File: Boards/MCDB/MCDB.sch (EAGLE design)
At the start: 57 parts, among them IC1 MC33926

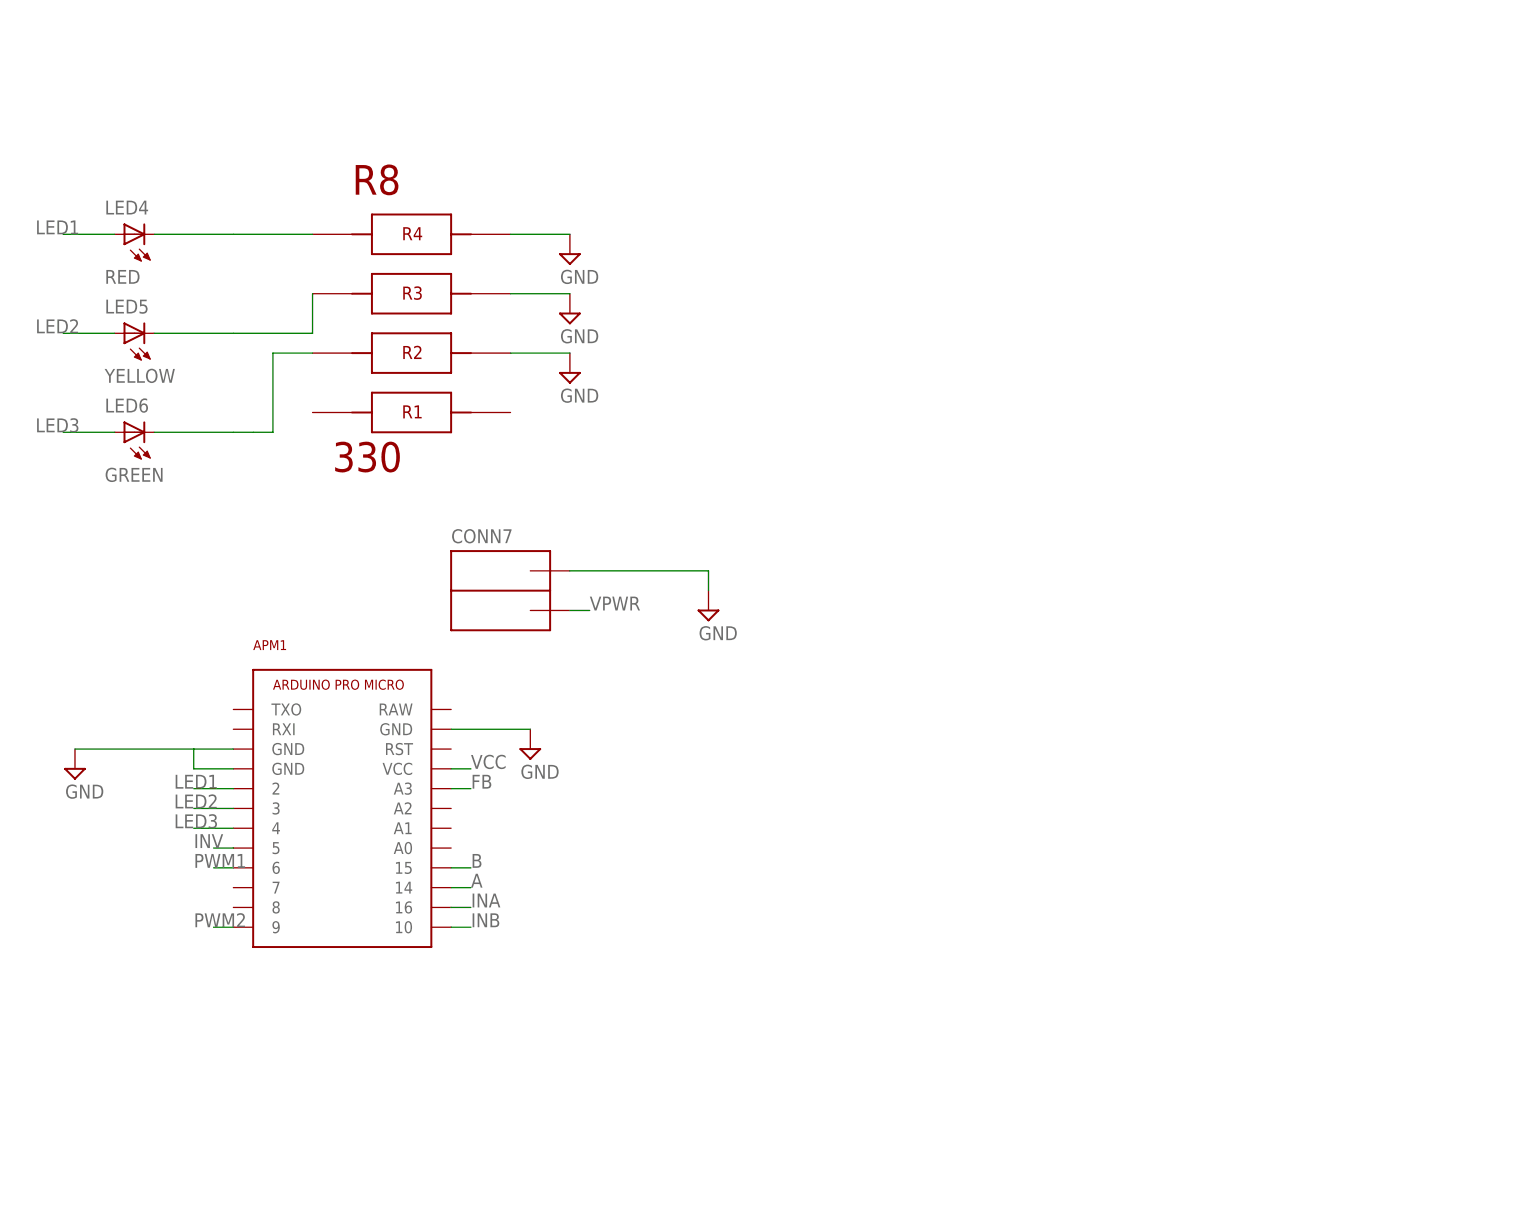
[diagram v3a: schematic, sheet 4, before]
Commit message: add 32U4 to mcdb schematic
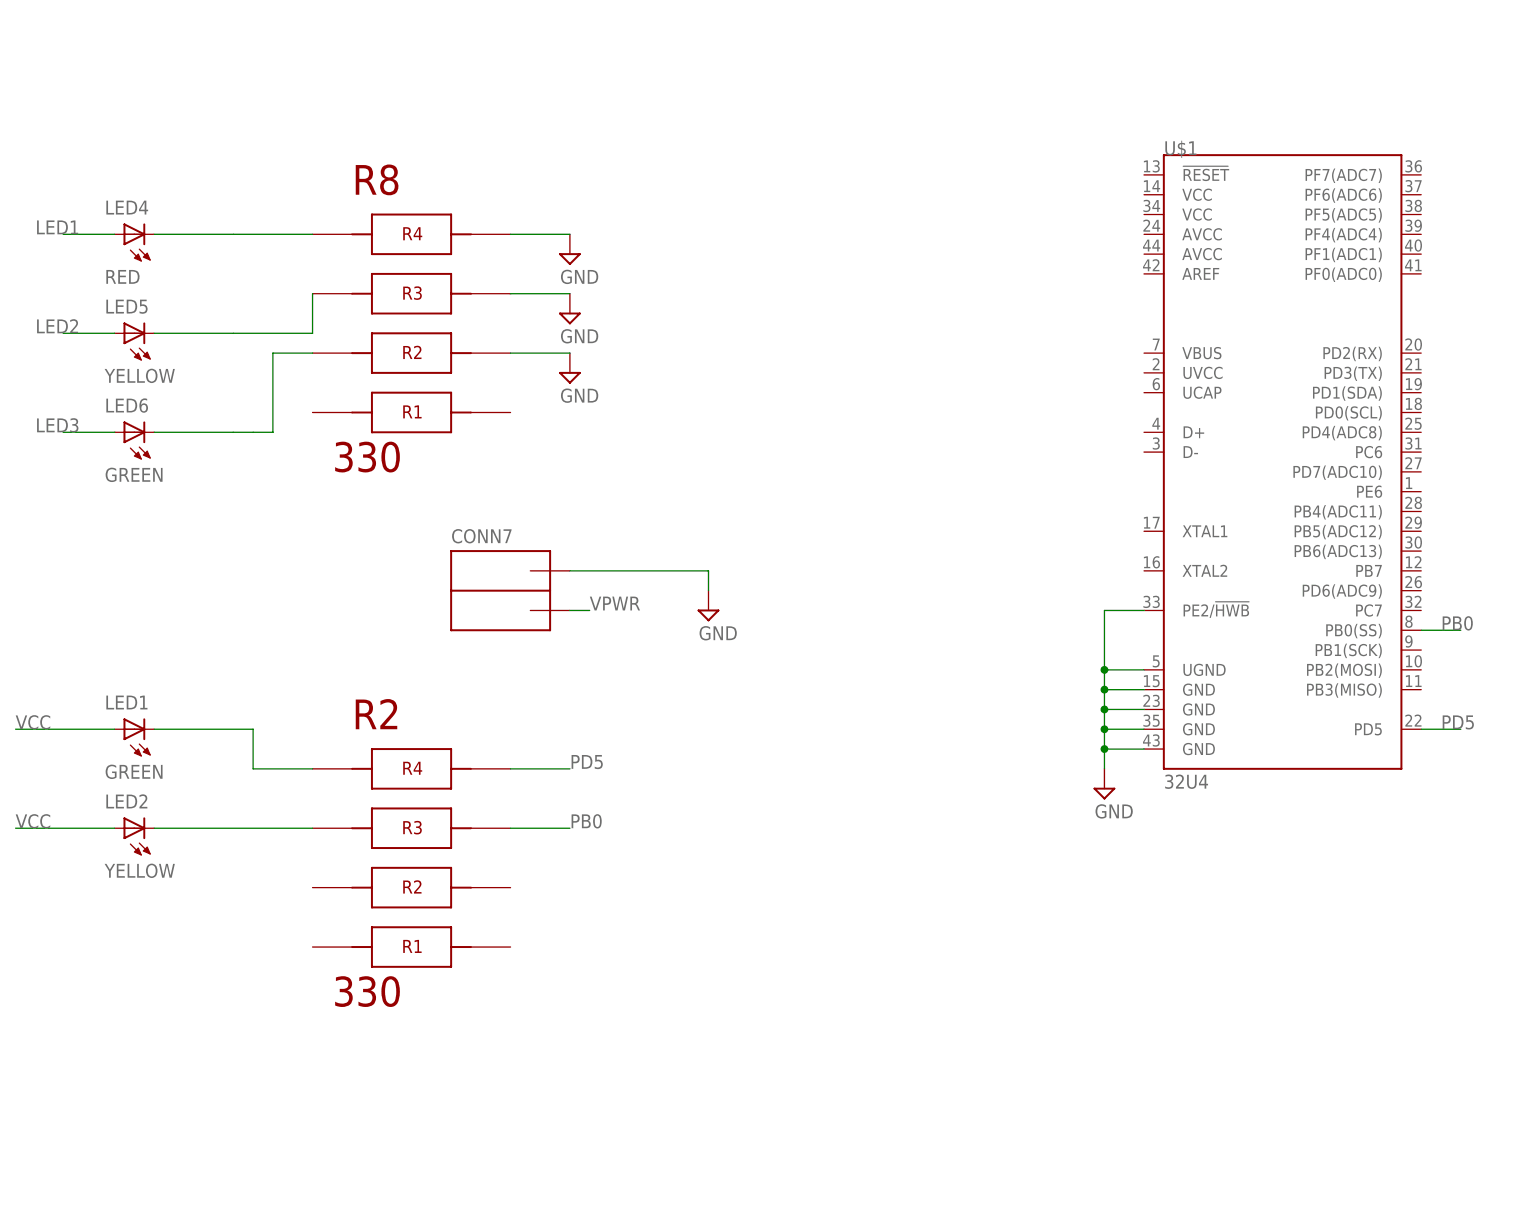
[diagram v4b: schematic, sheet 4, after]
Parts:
- removed APM1: ARDUINO_PRO_MICRO, pie:ARDUINO_PRO_MICRO
- added LED1: GREEN, pie:LED1206
- added LED2: YELLOW, pie:LED1206
- added R2: 330, pie:4X-0603
- added U$1: 32U4, SparkFun-IC-Microcontroller:ATMEGA32U4TQFP-44
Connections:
- removed net A: APM1.14
- removed net B: APM1.15
- removed net FB: APM1.A3
- removed net INA: APM1.16
- removed net INB: APM1.10
- removed net INV: APM1.5
- new net N$12: LED1.C, R2.5
- new net N$13: LED2.C, R2.6
- new net PB0: R2.3, U$1.PB0(SS)
- new net PD5: R2.4, U$1.PD5
- net GND: now also U$1.GND@15, U$1.GND@23, U$1.GND@35, U$1.GND@43, U$1.PE2/!HWB, U$1.UGND; no longer APM1.GND@0, APM1.GND@1, APM1.GND@2
- net LED1: no longer APM1.2
- net LED2: no longer APM1.3
- net LED3: no longer APM1.4
- net PWM1: no longer APM1.6
- net PWM2: no longer APM1.9
- net VCC: now also LED1.A, LED2.A; no longer APM1.VCC

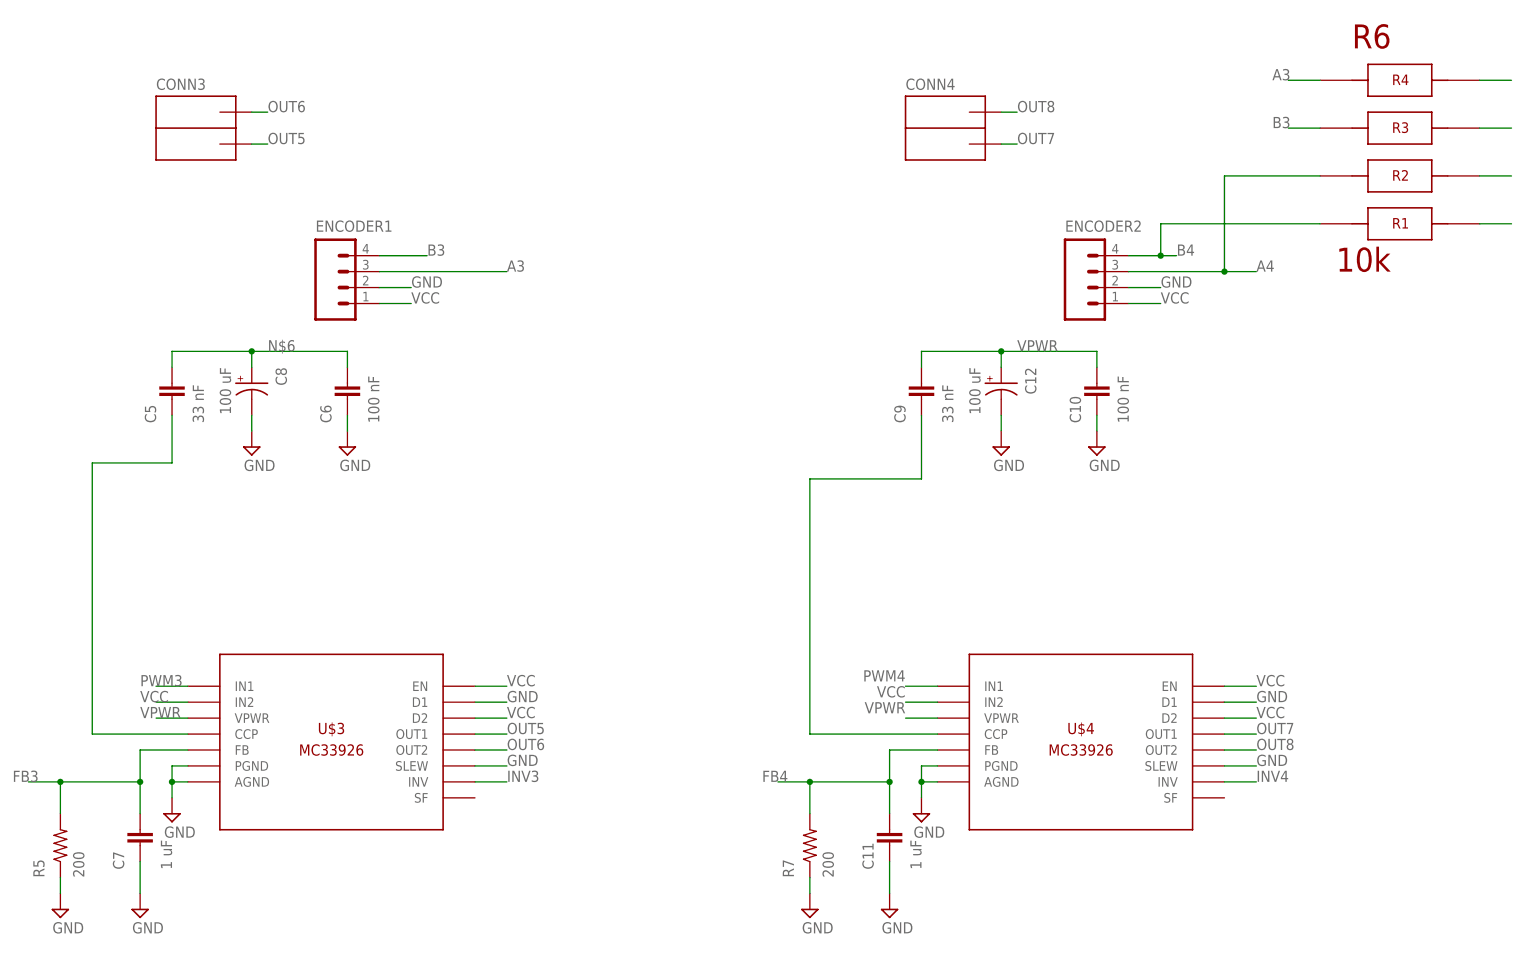
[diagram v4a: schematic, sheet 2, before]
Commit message: Added atmega32u4 to library
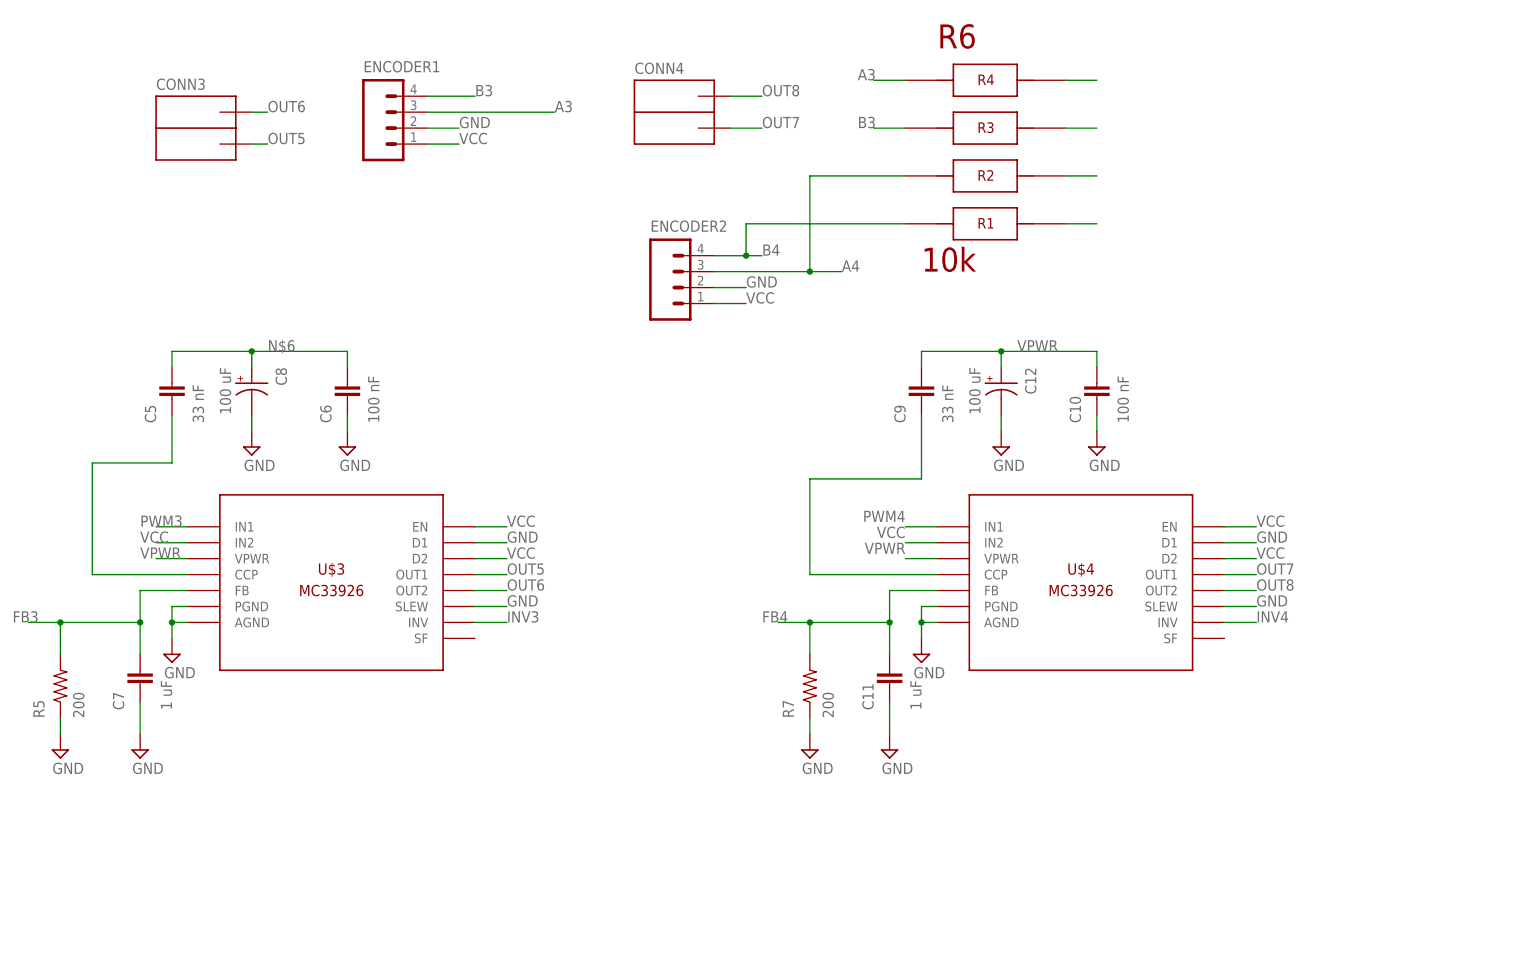
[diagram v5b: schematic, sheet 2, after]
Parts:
- U$1: device SparkFun-IC-Microcontroller:ATMEGA32U4TQFP-44 -> pie:ATMEGA32U4TQFP-44
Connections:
- new net N$16: U$1.VCC@14
- new net N$17: U$1.VCC@34
- new net N$18: U$1.AVCC@24
- new net N$19: U$1.AVCC@44
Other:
- moved on the sheet: C11, C15, C19, C23, C3, C7, CONN4, ENCODER1, ENCODER2, IC1, R11, R13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

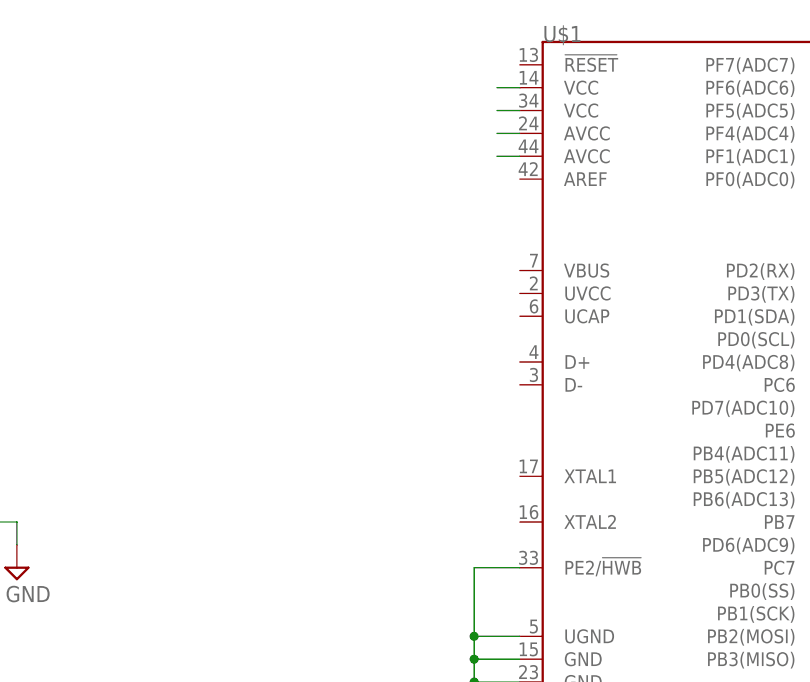
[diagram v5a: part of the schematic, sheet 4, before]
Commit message: added new crystal footprint
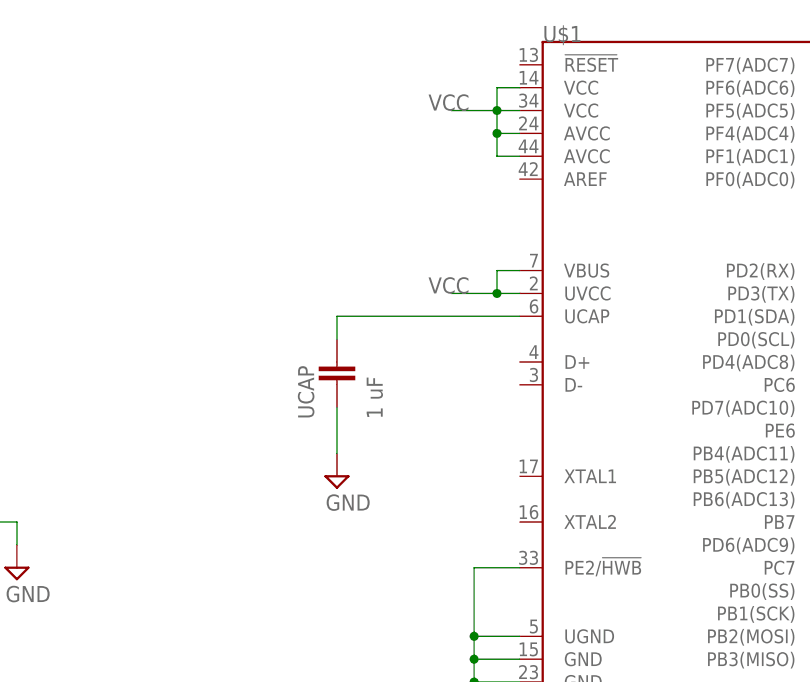
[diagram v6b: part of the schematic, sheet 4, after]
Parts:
- added UCAP: 1 uF, pie:CAP0603-CAP
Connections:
- removed net N$17: U$1.VCC@34
- removed net N$18: U$1.AVCC@24
- removed net N$19: U$1.AVCC@44
- net GND: now also UCAP.1
- net N$16: now also U$1.UCAP, UCAP.2; no longer U$1.VCC@14
- net VCC: now also U$1.AVCC@24, U$1.AVCC@44, U$1.UVCC, U$1.VBUS, U$1.VCC@14, U$1.VCC@34
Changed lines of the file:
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@@
 <part name="R2" library="pie" deviceset="4X-0603" device="" value="330"/>
 <part name="U$1" library="pie" deviceset="ATMEGA32U4" device="TQFP-44" package3d_urn="urn:adsk.eagle:package:38953/1" value="32U4"/>
+<part name="UCAP" library="pie" deviceset="CAP" device="0603-CAP" value="1 uF"/>
+<part name="SUPPLY15" library="pie" deviceset="GND" device=""/>
 </parts>
 <sheets>
@@
 <attribute name="NAME" x="157.48" y="160.02" size="1.778" layer="95"/>
 <attribute name="VALUE" x="157.48" y="78.74" size="1.778" layer="96"/>
+</instance>
+<instance part="UCAP" gate="G$1" x="134.62" y="121.92" smashed="yes" rot="R90">
+<attribute name="NAME" x="132.08" y="118.11" size="1.778" layer="95" rot="R90"/>
+<attribute name="VALUE" x="139.7" y="118.11" size="1.778" layer="96" rot="R90"/>
+</instance>
+<instance part="SUPPLY15" gate="GND" x="134.62" y="111.76" smashed="yes">
+<attribute name="VALUE" x="133.35" y="107.95" size="1.778" layer="96"/>
 </instance>
 </instances>
@@
 <pinref part="U$1" gate="G$1" pin="UGND"/>
 </segment>
+<segment>
+<pinref part="SUPPLY15" gate="GND" pin="GND"/>
+<pinref part="UCAP" gate="G$1" pin="1"/>
+<wire x1="134.62" y1="114.3" x2="134.62" y2="119.38" width="0.1524" layer="91"/>
+</segment>
 </net>
 <net name="LED1" class="0">
@@
 <label x="10.16" y="73.66" size="1.778" layer="95"/>
 </segment>
+<segment>
+<pinref part="U$1" gate="G$1" pin="AVCC@44"/>
+<wire x1="154.94" y1="147.32" x2="152.4" y2="147.32" width="0.1524" layer="91"/>
+<pinref part="U$1" gate="G$1" pin="AVCC@24"/>
+<wire x1="154.94" y1="149.86" x2="152.4" y2="149.86" width="0.1524" layer="91"/>
+<wire x1="152.4" y1="147.32" x2="152.4" y2="149.86" width="0.1524" layer="91"/>
+<pinref part="U$1" gate="G$1" pin="VCC@34"/>
+<wire x1="154.94" y1="152.4" x2="152.4" y2="152.4" width="0.1524" layer="91"/>
+<wire x1="152.4" y1="149.86" x2="152.4" y2="152.4" width="0.1524" layer="91"/>
+<junction x="152.4" y="149.86"/>
+<pinref part="U$1" gate="G$1" pin="VCC@14"/>
+<wire x1="154.94" y1="154.94" x2="152.4" y2="154.94" width="0.1524" layer="91"/>
+<wire x1="152.4" y1="152.4" x2="152.4" y2="154.94" width="0.1524" layer="91"/>
+<junction x="152.4" y="152.4"/>
+<wire x1="152.4" y1="152.4" x2="147.32" y2="152.4" width="0.1524" layer="91"/>
+<label x="144.78" y="152.4" size="1.778" layer="95"/>
+</segment>
+<segment>
+<pinref part="U$1" gate="G$1" pin="VBUS"/>
+<wire x1="154.94" y1="134.62" x2="152.4" y2="134.62" width="0.1524" layer="91"/>
+<pinref part="U$1" gate="G$1" pin="UVCC"/>
+<wire x1="154.94" y1="132.08" x2="152.4" y2="132.08" width="0.1524" layer="91"/>
+<wire x1="152.4" y1="132.08" x2="152.4" y2="134.62" width="0.1524" layer="91"/>
+<junction x="152.4" y="132.08"/>
+<wire x1="152.4" y1="132.08" x2="147.32" y2="132.08" width="0.1524" layer="91"/>
+<label x="144.78" y="132.08" size="1.778" layer="95"/>
+</segment>
 </net>
 <net name="PD5" class="0">
@@
 <net name="N$16" class="0">
 <segment>
-<pinref part="U$1" gate="G$1" pin="VCC@14"/>
-<wire x1="154.94" y1="154.94" x2="152.4" y2="154.94" width="0.1524" layer="91"/>
-</segment>
-</net>
-<net name="N$17" class="0">
-<segment>
-<pinref part="U$1" gate="G$1" pin="VCC@34"/>
-<wire x1="154.94" y1="152.4" x2="152.4" y2="152.4" width="0.1524" layer="91"/>
-</segment>
-</net>
-<net name="N$18" class="0">
-<segment>
-<pinref part="U$1" gate="G$1" pin="AVCC@24"/>
-<wire x1="154.94" y1="149.86" x2="152.4" y2="149.86" width="0.1524" layer="91"/>
-</segment>
-</net>
-<net name="N$19" class="0">
-<segment>
-<pinref part="U$1" gate="G$1" pin="AVCC@44"/>
-<wire x1="154.94" y1="147.32" x2="152.4" y2="147.32" width="0.1524" layer="91"/>
-</segment>
-</net>
+<pinref part="U$1" gate="G$1" pin="UCAP"/>
+<pinref part="UCAP" gate="G$1" pin="2"/>
+<wire x1="154.94" y1="129.54" x2="134.62" y2="129.54" width="0.1524" layer="91"/>
+<wire x1="134.62" y1="129.54" x2="134.62" y2="127" width="0.1524" layer="91"/>
+</segment>
+</net>
